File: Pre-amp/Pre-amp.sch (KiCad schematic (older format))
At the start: 78 parts, among them J1 In, J2 PWR, J3 Send, J4 Return, J5 Out, U1 LF353N, U2 LF353N, U3 LF353N, U4 LF353N

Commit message: add switching
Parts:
- added C17, C27: .047, Capacitor_THT:C_Disc_D3.8mm_W2.6mm_P2.50mm, symbol Device:C
- added C18, C22, C23, C25: 1, symbol Device:CP
- added C19, C20, C24: .1, Capacitor_THT:C_Disc_D3.8mm_W2.6mm_P2.50mm, symbol Device:C
- added C21: 560pf, Capacitor_THT:C_Disc_D3.8mm_W2.6mm_P2.50mm, symbol Device:C
- added C26, C28: .22, Capacitor_THT:C_Disc_D3.8mm_W2.6mm_P2.50mm, symbol Device:C
- added D5, D6, D7, D8: 1N4002, symbol Device:D
- added K1: G6H-2, symbol Relay:G6H-2
- added Q1, Q2: J113, symbol Device:Q_NJFET_SDG
- added Q3, Q4: J113 NJFET, symbol Device:Q_NJFET_SDG
- added R41, R45, R50: 33k, symbol Device:R
- added R42, R51: 25k, symbol Device:R_Variable_US
- added R43, R46, R47, R52, R53, R54: 220k, symbol Device:R
- added R44: 120k, symbol Device:R
- added R48, R55, R56: 3.3k, symbol Device:R
- added R49: 82k, symbol Device:R
- added R57: 12k, symbol Device:R
- added R58: 1k, symbol Device:R
- added RV6, RV7, RV8: 25k-A, Potentiometers:Potentiometer_Alps_RK163_Single_Vertical, symbol Device:R_POT_US
- added SW1: Jack, symbol Switch:SW_SPDT
- added SW?: Panel, symbol Switch:SW_SPDT
- added U5: LF353N, Package_DIP:DIP-8_W7.62mm_LongPads, symbol Pre-amp-rescue:LF353N-2019-03-05_16-55-55
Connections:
- net +15V: now also R58.1, U5.8 (V+)
- net -15V: now also U5.4 (V-)
- net GND: now also U4.5 (IN+), C18.2, C19.2, C23.2, D5.1 (K), D6.2 (A), D7.1 (K), D8.2 (A), R44.2, R46.2, R56.2, RV6.3, RV7.3, RV8.3, SW1.2 (B), SW?.2 (B)
- net at R15.2, R16.2: now also K1.3; no longer R14.1, RV1.1
- net at R6.1, R7.2: now also K1.8; no longer C5.1, R8.2
- net at U4.6 (IN-): now also U4.7 (OUT)
- new net: C5.1, K1.7, R8.2
- new net: K1.4, R14.1, RV1.1
- new net: K1.1, R58.2
- new net: K1.10, SW1.1 (A), SW?.1 (A)
- new net: K1.2, RV8.2
- new net: C17.1, K1.9, R44.1
- new net: C17.2, RV6.1
- new net: D5.2 (A), D6.1 (K), Q1.3 (G), RV6.2
- new net: Q1.1 (S), Q2.1 (S), R43.1
- new net: C21.2, Q1.2 (D), R42.2, R49.2, U5.2 (IN-)
- new net: R41.2, R42.1
- new net: C20.1, C21.1, C22.1, R47.1, U5.1 (OUT)
- new net: C20.2, R48.1
- new net: R48.2, RV7.1
- new net: D7.2 (A), D8.1 (K), Q3.3 (G), RV7.2
- new net: Q3.1 (S), Q4.1 (S), R52.1
- new net: C24.2, Q3.2 (D), R51.2, R54.2, U5.6 (IN-)
- new net: C23.1, Q4.3 (G), R53.2
- new net: R50.2, R51.1
- new net: C24.1, C25.1, C27.1, R53.1, R55.1, U5.7 (OUT)
- new net: C27.2, R57.1, RV8.1
- new net: C22.2, R49.1
- new net: C25.2, R54.1
- new net: C26.2, C28.1, R55.2
- new net: C26.1, R56.1
- new net: C28.2, R57.2
- new net D: Q2.2 (D), Q4.2 (D), R41.1, R45.1, R50.1
- new net E: R43.2, R52.2
- new net F: C18.1, C19.1, Q2.3 (G), R45.2, R46.1, R47.2, U5.3 (IN+), U5.5 (IN+)
- no-connect marks 6 -> 3
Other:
- moved on the sheet: C1, C10, C11, C12, C13, C14, C15, C16, C2, C3, C4, C5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

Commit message: Fix errors found in build. Change version to 1.2.0
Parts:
- C14: value .47 -> .047uf
- R2: value 23k -> 22k
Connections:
- net GND: now also D2.2 (A); no longer D2.1 (K)
- net at D1.1 (K): now also D2.1 (K); no longer D2.2 (A)
- net at R37.1, U4.3 (IN+): now also D3.1 (K); no longer D3.2 (A)
- net at D4.2 (A): now also D3.2 (A); no longer D3.1 (K)
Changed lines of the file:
@@
 encoding utf-8
 Sheet 1 1
-Title "preamp"
-Date "2019-04-01"
-Rev "1.1.1"
+Title "preamp w/Dist"
+Date "2019-04-27"
+Rev "1.2.0"
 Comp "MXM Designs"
 Comment1 ""
@@
 U 1 1 5C7FE300
 P 8000 3550
-F 0 "C8" H 8115 3596 50  0000 L CNN
-F 1 "560pF" H 8115 3505 50  0000 L CNN
+F 0 "C8" H 7800 3600 50  0000 L CNN
+F 1 "560pF" H 8100 3600 50  0000 L CNN
 F 2 "Capacitor_THT:C_Disc_D3.8mm_W2.6mm_P2.50mm" H 8038 3400 50  0001 C CNN
 F 3 "~" H 8000 3550 50  0001 C CNN
@@
 U 1 1 5C7FE3E3
 P 9750 3600
-F 0 "C10" H 9865 3646 50  0000 L CNN
-F 1 ".0022" H 9865 3555 50  0000 L CNN
+F 0 "C10" H 9500 3650 50  0000 L CNN
+F 1 ".0022" H 9850 3650 50  0000 L CNN
 F 2 "Capacitor_THT:C_Disc_D3.8mm_W2.6mm_P2.50mm" H 9788 3450 50  0001 C CNN
 F 3 "~" H 9750 3600 50  0001 C CNN
@@
 U 1 1 5C7FE4FC
 P 11350 3600
-F 0 "C12" H 11465 3646 50  0000 L CNN
-F 1 ".01" H 11465 3555 50  0000 L CNN
+F 0 "C12" H 11100 3650 50  0000 L CNN
+F 1 ".01" H 11450 3650 50  0000 L CNN
 F 2 "Capacitor_THT:C_Disc_D3.8mm_W2.6mm_P2.50mm" H 11388 3450 50  0001 C CNN
 F 3 "~" H 11350 3600 50  0001 C CNN
@@
 P 13150 3600
 F 0 "C14" H 13265 3646 50  0000 L CNN
-F 1 ".47" H 13265 3555 50  0000 L CNN
+F 1 ".047uf" H 13265 3555 50  0000 L CNN
 F 2 "Capacitor_THT:C_Disc_D3.8mm_W2.6mm_P2.50mm" H 13188 3450 50  0001 C CNN
 F 3 "~" H 13150 3600 50  0001 C CNN
@@
 F 3 "~" H 13800 5800 50  0001 C CNN
 	1    13800 5800
-	0    -1   -1   0
+	0    1    1    0
 $EndComp
 $Comp
@@
 P 1650 2250
 F 0 "R2" V 1443 2250 50  0000 C CNN
-F 1 "23k" V 1534 2250 50  0000 C CNN
+F 1 "22k" V 1534 2250 50  0000 C CNN
 F 2 "Resistor_THT:R_Axial_DIN0207_L6.3mm_D2.5mm_P7.62mm_Horizontal" V 1580 2250 50  0001 C CNN
 F 3 "~" H 1650 2250 50  0001 C CNN
@@
 F 3 "~" H 1900 3800 50  0001 C CNN
 	1    1900 3800
-	0    -1   -1   0
-$EndComp
-$Comp
+	0    1    1    0
+$EndComp
+$Comp

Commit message: update schematic symbols
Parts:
- removed C6: 10, Capacitor_THT:C_Disc_D3.8mm_W2.6mm_P2.50mm, symbol Device:C
- added C6: 10uf, Capacitor_THT:CP_Radial_D4.0mm_P1.50mm, symbol Device:CP
- C1, C15, C16, C19, C20, C24: value .1 -> 0.1uf
- C10, C9: value .0022 -> 0.0022uf
- C11, C12: value .01 -> 0.01uf
- C13, C17, C27: value .047 -> 0.047uf
- C14: value .047uf -> 0.047uf
- C18, C22, C23, C25: value 1 -> 1uf; footprint (none) -> Capacitor_THT:C_Disc_D3.8mm_W2.6mm_P2.50mm
- C26, C28, C4: value .22 -> 0.22uf
- C3: value 10µF -> 10uf
- C5: value .0033 -> 0.0033uf
- C8: value 560pF -> 560pf
- D5, D6, D7, D8: footprint (none) -> Diode_THT:D_DO-41_SOD81_P7.62mm_Horizontal
- Q1, Q2: value J113 -> J113 NJFET; footprint (none) -> Package_TO_SOT_THT:TO-92
- Q3, Q4: footprint (none) -> Package_TO_SOT_THT:TO-92
- R41, R42, R43, R44, R45, R46, R47, R48, R49, R50, R51, R52, R53, R54, R55, R56, R57, R58: footprint (none) -> Resistor_THT:R_Axial_DIN0207_L6.3mm_D2.5mm_P7.62mm_Horizontal
- SW1: footprint (none) -> digikey-footprints:Switch_Toggle_ATE1D-2M3-10-Z
- SW2: renamed from SW?; footprint (none) -> digikey-footprints:Switch_Toggle_ATE1D-2M3-10-Z
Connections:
- net at R8.1, R9.2: now also R10.1, R11.2
- net at R12.1: now also C6.1
- net at RV1.3: now also C6.2

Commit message: update schematic symbols
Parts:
- added C29, C30: 0.01uf, Capacitor_THT:C_Disc_D3.8mm_W2.6mm_P2.50mm, symbol Device:C
- added C31, C32: 10uf, Capacitor_THT:CP_Radial_D4.0mm_P1.50mm, symbol Device:CP
- added D9: 1N4002, Diode_THT:D_DO-41_SOD81_P7.62mm_Horizontal, symbol Device:D
- added R59, R60: 3.3k, Resistor_THT:R_Axial_DIN0207_L6.3mm_D2.5mm_P7.62mm_Horizontal, symbol Device:R
- added R61: 1k, Resistor_THT:R_Axial_DIN0207_L6.3mm_D2.5mm_P7.62mm_Horizontal, symbol Device:R
- C24: value 0.1uf -> 100pf
- C27: value 0.047uf -> 0.0047uf
- R54: value 220k -> 270k
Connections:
- net D: now also C31.1, R59.1
- net E: now also C32.2, R60.1
- net GND: now also C29.2, C30.1, C31.2, C32.1, D9.2 (A)
- net at C20.1, C21.1, R47.1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: now also C22.2; no longer C22.1
- net at C24.1, C27.1, R53.1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: now also C25.2; no longer C25.1
- net at R49.1: now also C22.1; no longer C22.2
- net at R54.1: now also C25.1; no longer C25.2
- new net: D9.1 (K), R61.1
- new net B: C29.1, R59.2
- new net C: C30.2, R60.2, R61.2
- no-connect marks 3 -> 5
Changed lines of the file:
@@
 F 3 "~" H 5500 6400 50  0001 C CNN
 	1    5500 6400
-	0    1    1    0
+	0    -1   -1   0
 $EndComp
 Wire Wire Line
@@
 P 8300 7650
 F 0 "C24" V 8000 7650 50  0000 C CNN
-F 1 "0.1uf" V 8150 7650 50  0000 C CNN
+F 1 "100pf" V 8150 7650 50  0000 C CNN
 F 2 "Capacitor_THT:C_Disc_D3.8mm_W2.6mm_P2.50mm" H 8338 7500 50  0001 C CNN
 F 3 "~" H 8300 7650 50  0001 C CNN
@@
 F 3 "~" H 8550 8000 50  0001 C CNN
 	1    8550 8000
-	0    1    1    0
+	0    -1   -1   0
 $EndComp
 $Comp
@@
 P 8100 8000
 F 0 "R54" V 7893 8000 50  0000 C CNN
-F 1 "220k" V 7984 8000 50  0000 C CNN
+F 1 "270k" V 7984 8000 50  0000 C CNN
 F 2 "Resistor_THT:R_Axial_DIN0207_L6.3mm_D2.5mm_P7.62mm_Horizontal" V 8030 8000 50  0001 C CNN
 F 3 "~" H 8100 8000 50  0001 C CNN
@@
 P 9350 8900
 F 0 "C27" V 9200 8900 50  0000 C CNN
-F 1 "0.047uf" V 9500 8900 50  0000 C CNN
+F 1 "0.0047uf" V 9500 8900 50  0000 C CNN
 F 2 "Capacitor_THT:C_Disc_D3.8mm_W2.6mm_P2.50mm" H 9388 8750 50  0001 C CNN
 F 3 "~" H 9350 8900 50  0001 C CNN
@@
 Wire Wire Line
 	5800 4700 5800 4750
+NoConn ~ 2550 4850
+NoConn ~ 2550 5250
+$Comp
+L Device:R R59
+U 1 1 5CDABE09
+P 11150 7150
+F 0 "R59" V 10943 7150 50  0000 C CNN
+F 1 "3.3k" V 11034 7150 50  0000 C CNN
+F 2 "Resistor_THT:R_Axial_DIN0207_L6.3mm_D2.5mm_P7.62mm_Horizontal" V 11080 7150 50  0001 C CNN
+F 3 "~" H 11150 7150 50  0001 C CNN
+	1    11150 7150
+	0    1    1    0
+$EndComp
+$Comp
+L Device:R R60
+U 1 1 5CDAC229
+P 11150 8400
+F 0 "R60" V 10943 8400 50  0000 C CNN
+F 1 "3.3k" V 11034 8400 50  0000 C CNN
+F 2 "Resistor_THT:R_Axial_DIN0207_L6.3mm_D2.5mm_P7.62mm_Horizontal" V 11080 8400 50  0001 C CNN
+F 3 "~" H 11150 8400 50  0001 C CNN
+	1    11150 8400
+	0    1    1    0
+$EndComp
+$Comp
+L Device:CP C31
+U 1 1 5CDAC3E8
+P 11650 7400
+F 0 "C31" H 11800 7300 50  0000 C CNN
+F 1 "10uf" H 11800 7500 50  0000 C CNN
+F 2 "Capacitor_THT:CP_Radial_D4.0mm_P1.50mm" H 11688 7250 50  0001 C CNN
+F 3 "~" H 11650 7400 50  0001 C CNN
+	1    11650 7400
+	1    0    0    -1
+$EndComp
+$Comp
+L Device:CP C32
+U 1 1 5CDACA0C
+P 11650 8100
+F 0 "C32" H 11800 7950 50  0000 C CNN
+F 1 "10uf" H 11800 8250 50  0000 C CNN
+F 2 "Capacitor_THT:CP_Radial_D4.0mm_P1.50mm" H 11688 7950 50  0001 C CNN
+F 3 "~" H 11650 8100 50  0001 C CNN
+	1    11650 8100
+	1    0    0    -1
+$EndComp
+$Comp
+L Device:C C29
+U 1 1 5CDAD6B5
+P 10650 7400
+F 0 "C29" H 10850 7300 50  0000 C CNN
+F 1 "0.01uf" H 10800 7500 50  0000 C CNN
+F 2 "Capacitor_THT:C_Disc_D3.8mm_W2.6mm_P2.50mm" H 10688 7250 50  0001 C CNN
+F 3 "~" H 10650 7400 50  0001 C CNN
+	1    10650 7400
+	1    0    0    -1
+$EndComp
+$Comp
+L Device:C C30
+U 1 1 5CDADB14
+P 10650 8100
+F 0 "C30" H 10850 8000 50  0000 C CNN
+F 1 "0.01uf" H 10800 8200 50  0000 C CNN
+F 2 "Capacitor_THT:C_Disc_D3.8mm_W2.6mm_P2.50mm" H 10688 7950 50  0001 C CNN
+F 3 "~" H 10650 8100 50  0001 C CNN
+	1    10650 8100
+	1    0    0    -1
+$EndComp
+$Comp
+L Device:R R61
+U 1 1 5CE0A934
+P 11150 8750
+F 0 "R61" V 10943 8750 50  0000 C CNN
+F 1 "1k" V 11034 8750 50  0000 C CNN
+F 2 "Resistor_THT:R_Axial_DIN0207_L6.3mm_D2.5mm_P7.62mm_Horizontal" V 11080 8750 50  0001 C CNN
+F 3 "~" H 11150 8750 50  0001 C CNN
+	1    11150 8750
+	0    1    1    0
+$EndComp
+Wire Wire Line
+	10650 7250 10650 7150
+Wire Wire Line
+	10650 7150 11000 7150
+Wire Wire Line
+	11300 7150 11650 7150
+Wire Wire Line
+	11650 7150 11650 7250
+Wire Wire Line
+	11650 7550 11650 7750
+Wire Wire Line
+	10650 7550 10650 7750
+Wire Wire Line
+	10650 8250 10650 8400
+Wire Wire Line
+	10650 8400 11000 8400
+Wire Wire Line
+	11300 8400 11650 8400
+Wire Wire Line
+	11650 8400 11650 8250
+Wire Wire Line
+	11000 8750 10650 8750
+Wire Wire Line
+	10650 8750 10650 8400
+Connection ~ 10650 8400
+Wire Wire Line
+	10650 7750 11650 7750
+Connection ~ 10650 7750
+Wire Wire Line
+	10650 7750 10650 7950
+Connection ~ 11650 7750
+Wire Wire Line
+	11650 7750 11650 7950
+$Comp
+L power:GND #PWR033
+U 1 1 5CF82DD3
+P 12150 7800
+F 0 "#PWR033" H 12150 7550 50  0001 C CNN
+F 1 "GND" H 12155 7627 50  0000 C CNN
+F 2 "" H 12150 7800 50  0001 C CNN
+F 3 "" H 12150 7800 50  0001 C CNN
+	1    12150 7800
+	1    0    0    -1
+$EndComp
+Wire Wire Line
+	11650 7750 12150 7750
+Wire Wire Line
+	12150 7750 12150 7800
+$Comp
+L Device:D D9
+U 1 1 5CFB3B2A
+P 11650 8750
+F 0 "D9" H 11650 8966 50  0000 C CNN
+F 1 "1N4002" H 11650 8875 50  0000 C CNN
+F 2 "Diode_THT:D_DO-41_SOD81_P7.62mm_Horizontal" H 11650 8750 50  0001 C CNN
+F 3 "~" H 11650 8750 50  0001 C CNN
+	1    11650 8750
+	1    0    0    -1
+$EndComp
+Wire Wire Line
+	11500 8750 11300 8750
+$Comp
+L power:GND #PWR032
+U 1 1 5D018DF0
+P 12100 8900
+F 0 "#PWR032" H 12100 8650 50  0001 C CNN
+F 1 "GND" H 12105 8727 50  0000 C CNN
+F 2 "" H 12100 8900 50  0001 C CNN
+F 3 "" H 12100 8900 50  0001 C CNN
+	1    12100 8900
+	1    0    0    -1
+$EndComp
+Wire Wire Line
+	11800 8750 12100 8750
+Wire Wire Line
+	12100 8750 12100 8900
+Wire Wire Line
+	11650 8400 11900 8400
+Connection ~ 11650 8400
+Text GLabel 11900 8400 2    50   Input ~ 0
+E
+Wire Wire Line
+	10650 7150 10450 7150
+Connection ~ 10650 7150
+Wire Wire Line
+	11650 7150 11950 7150
+Connection ~ 11650 7150
+Text GLabel 11950 7150 2    50   Input ~ 0
+D
+Text GLabel 10450 7150 0    50   Input ~ 0
+B
+Wire Wire Line
+	10650 8400 10400 8400
+Text GLabel 10400 8400 0    50   Input ~ 0
+C
 $EndSCHEMATC

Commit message: update schematic for distortion section
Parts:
- RV1, RV2, RV3, RV4, RV5, RV6, RV7, RV8: footprint Potentiometers:Potentiometer_Alps_RK163_Single_Vertical -> Potentiometer_THT:Potentiometer_Alps_RK163_Single_Horizontal
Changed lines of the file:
@@
 F 0 "RV2" V 7795 3050 50  0000 C CNN
 F 1 "25k-L" V 7886 3050 50  0000 C CNN
-F 2 "Potentiometers:Potentiometer_Alps_RK163_Single_Vertical" H 8000 3050 50  0001 C CNN
+F 2 "Potentiometer_THT:Potentiometer_Alps_RK163_Single_Horizontal" H 8000 3050 50  0001 C CNN
 F 3 "~" H 8000 3050 50  0001 C CNN
 	1    8000 3050
@@
 F 0 "RV3" V 9545 2100 50  0000 C CNN
 F 1 "25k-A" V 9636 2100 50  0000 C CNN
-F 2 "Potentiometers:Potentiometer_Alps_RK163_Single_Vertical" H 9750 2100 50  0001 C CNN
+F 2 "Potentiometer_THT:Potentiometer_Alps_RK163_Single_Horizontal" H 9750 2100 50  0001 C CNN
 F 3 "~" H 9750 2100 50  0001 C CNN
 	1    9750 2100
@@
 F 0 "RV4" V 11145 3100 50  0000 C CNN
 F 1 "25k-L" V 11236 3100 50  0000 C CNN
-F 2 "Potentiometers:Potentiometer_Alps_RK163_Single_Vertical" H 11350 3100 50  0001 C CNN
+F 2 "Potentiometer_THT:Potentiometer_Alps_RK163_Single_Horizontal" H 11350 3100 50  0001 C CNN
 F 3 "~" H 11350 3100 50  0001 C CNN
 	1    11350 3100
@@
 F 0 "RV5" V 12945 3100 50  0000 C CNN
 F 1 "25k-L" V 13036 3100 50  0000 C CNN
-F 2 "Potentiometers:Potentiometer_Alps_RK163_Single_Vertical" H 13150 3100 50  0001 C CNN
+F 2 "Potentiometer_THT:Potentiometer_Alps_RK163_Single_Horizontal" H 13150 3100 50  0001 C CNN
 F 3 "~" H 13150 3100 50  0001 C CNN
 	1    13150 3100
@@
 F 0 "RV1" V 6095 2650 50  0000 C CNN
 F 1 "25k-L" V 6186 2650 50  0000 C CNN
-F 2 "Potentiometers:Potentiometer_Alps_RK163_Single_Vertical" H 6300 2650 50  0001 C CNN
+F 2 "Potentiometer_THT:Potentiometer_Alps_RK163_Single_Horizontal" H 6300 2650 50  0001 C CNN
 F 3 "~" H 6300 2650 50  0001 C CNN
 	1    6300 2650
@@
 F 0 "RV6" V 1645 7650 50  0000 C CNN
 F 1 "25k-A" V 1736 7650 50  0000 C CNN
-F 2 "Potentiometers:Potentiometer_Alps_RK163_Single_Vertical" H 1850 7650 50  0001 C CNN
+F 2 "Potentiometer_THT:Potentiometer_Alps_RK163_Single_Horizontal" H 1850 7650 50  0001 C CNN
 F 3 "~" H 1850 7650 50  0001 C CNN
 	1    1850 7650
@@
 F 0 "RV7" V 4595 8900 50  0000 C CNN
 F 1 "25k-A" V 4686 8900 50  0000 C CNN
-F 2 "Potentiometers:Potentiometer_Alps_RK163_Single_Vertical" H 4800 8900 50  0001 C CNN
+F 2 "Potentiometer_THT:Potentiometer_Alps_RK163_Single_Horizontal" H 4800 8900 50  0001 C CNN
 F 3 "~" H 4800 8900 50  0001 C CNN
 	1    4800 8900
@@
 F 0 "RV8" V 6795 5950 50  0000 C CNN
 F 1 "25k-A" V 6886 5950 50  0000 C CNN
-F 2 "Potentiometers:Potentiometer_Alps_RK163_Single_Vertical" H 7000 5950 50  0001 C CNN
+F 2 "Potentiometer_THT:Potentiometer_Alps_RK163_Single_Horizontal" H 7000 5950 50  0001 C CNN
 F 3 "~" H 7000 5950 50  0001 C CNN
 	1    7000 5950

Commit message: place all components
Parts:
- K1: footprint (none) -> Relay_THT:Relay_DPDT_Omron_G6H-2
- R42, R51: footprint Resistor_THT:R_Axial_DIN0207_L6.3mm_D2.5mm_P7.62mm_Horizontal -> Potentiometer_THT:Potentiometer_Bourns_3386F_Vertical
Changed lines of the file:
@@
 F 0 "K1" V 5617 4900 50  0000 C CNN
 F 1 "G6H-2" V 5526 4900 50  0000 C CNN
-F 2 "" H 5300 4800 50  0001 C CNN
+F 2 "Relay_THT:Relay_DPDT_Omron_G6H-2" H 5300 4800 50  0001 C CNN
 F 3 "http://cdn-reichelt.de/documents/datenblatt/C300/G6H%23OMR.pdf" H 5500 5050 50  0001 C CNN
 	1    4850 4900
@@
 F 0 "R42" H 3428 7246 50  0000 L CNN
 F 1 "25k" H 3428 7155 50  0000 L CNN
-F 2 "Resistor_THT:R_Axial_DIN0207_L6.3mm_D2.5mm_P7.62mm_Horizontal" V 3230 7200 50  0001 C CNN
+F 2 "Potentiometer_THT:Potentiometer_Bourns_3386F_Vertical" V 3230 7200 50  0001 C CNN
 F 3 "~" H 3300 7200 50  0001 C CNN
 	1    3300 7200
@@
 F 0 "R51" H 6378 8496 50  0000 L CNN
 F 1 "25k" H 6378 8405 50  0000 L CNN
-F 2 "Resistor_THT:R_Axial_DIN0207_L6.3mm_D2.5mm_P7.62mm_Horizontal" V 6180 8450 50  0001 C CNN
+F 2 "Potentiometer_THT:Potentiometer_Bourns_3386F_Vertical" V 6180 8450 50  0001 C CNN
 F 3 "~" H 6250 8450 50  0001 C CNN
 	1    6250 8450

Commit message: get all parts on the board
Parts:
- R1, R10, R11, R12, R13, R14, R15, R16, R17, R18, R19, R2, R20, R21, R22, R23, R24, R25, R26, R27, R28, R29, R3, R30, R31, R32, R33, R34, R35, R36, R37, R38, R39, R4, R40, R41, R43, R44, R45, R46, R47, R48, R49, R5, R50, R52, R53, R54, R55, R56, R57, R58, R59, R6, R60, R61, R7, R8, R9: footprint Resistor_THT:R_Axial_DIN0207_L6.3mm_D2.5mm_P7.62mm_Horizontal -> Resistor_THT:R_Axial_DIN0204_L3.6mm_D1.6mm_P5.08mm_Horizontal

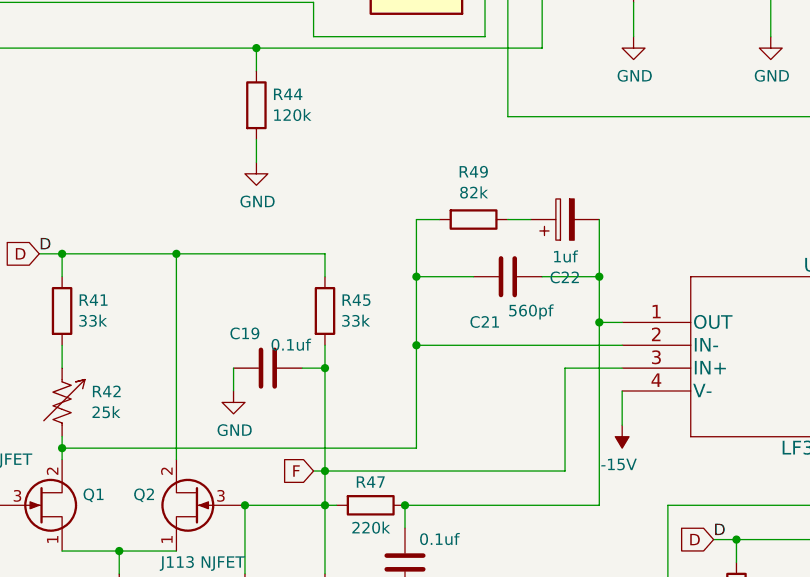
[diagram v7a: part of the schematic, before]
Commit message: update the schematic and PCB for lead section.
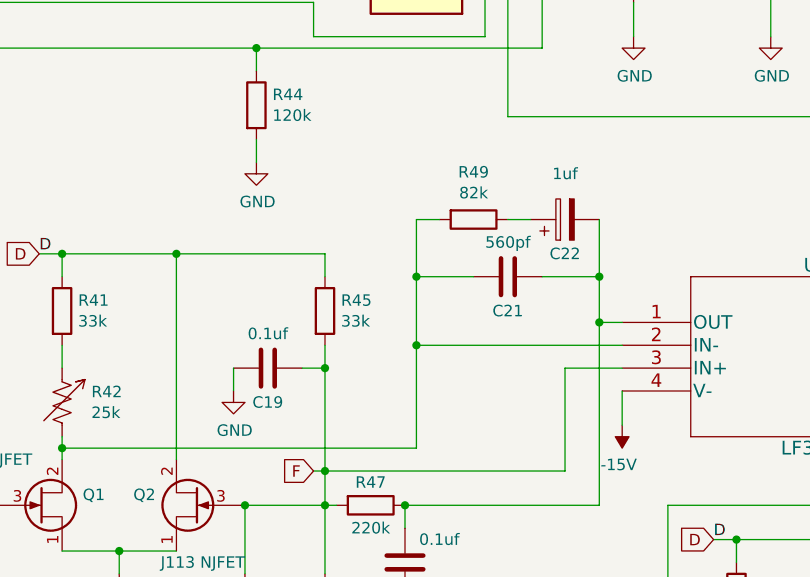
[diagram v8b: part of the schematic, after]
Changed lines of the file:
@@
 U 1 1 5CED677F
 P 4200 7050
-F 0 "C19" V 4050 6950 50  0000 C CNN
-F 1 "0.1uf" V 4100 7150 50  0000 C CNN
+F 0 "C19" V 4350 7050 50  0000 C CNN
+F 1 "0.1uf" V 4050 7050 50  0000 C CNN
 F 2 "Capacitor_THT:C_Disc_D3.8mm_W2.6mm_P2.50mm" H 4238 6900 50  0001 C CNN
 F 3 "~" H 4200 7050 50  0001 C CNN
@@
 U 1 1 5D23F8C9
 P 5250 6650
-F 0 "C21" V 5450 6550 50  0000 C CNN
-F 1 "560pf" V 5400 6750 50  0000 C CNN
+F 0 "C21" V 5400 6650 50  0000 C CNN
+F 1 "560pf" V 5100 6650 50  0000 C CNN
 F 2 "Capacitor_THT:C_Disc_D3.8mm_W2.6mm_P2.50mm" H 5288 6500 50  0001 C CNN
 F 3 "~" H 5250 6650 50  0001 C CNN
@@
 U 1 1 5D2424A4
 P 5500 6400
-F 0 "C22" V 5245 6400 50  0000 C CNN
-F 1 "1uf" V 5336 6400 50  0000 C CNN
+F 0 "C22" V 5350 6400 50  0000 C CNN
+F 1 "1uf" V 5700 6400 50  0000 C CNN
 F 2 "Capacitor_THT:C_Disc_D3.8mm_W2.6mm_P2.50mm" H 5538 6250 50  0001 C CNN
 F 3 "~" H 5500 6400 50  0001 C CNN
